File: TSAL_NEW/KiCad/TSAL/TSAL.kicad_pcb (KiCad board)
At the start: 2 copper layers, 74.8 x 40.6 mm, 34 parts, among them J1 HV INPUT, J2 HV GND, J3 Pin Storage, J4 Green_LED_Jp, J5 Conn_02x02_Counter_Clockwise, Q1 BSS84, Q2 BSS84, U1 LTV-817S, U2 LR8K4-G, U4 LM555

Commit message: TSAL Review complete
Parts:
- removed J5: Conn_02x02_Counter_Clockwise, Connector_TE-Connectivity:TE_MATE-N-LOK_1-770874-x_2x02_P4.14mm_Vertical
- added F2: Fuse, TSAL:PCC-1_2-R, F.Cu at (134.9, 90.7)
- added REF**: JUMPER_BLUE, TSAL:JUMPER_BLUE, F.Cu at (153.4, 105.2)
- added Ref**: Val**, TSAL:blinky, B.Cu at (166.9, 109.0)
- added Ref**: Val**, TSAL:zap, B.Cu at (125.5, 91.9)
- added Ref**: Val**, TSAL:zap, F.Cu at (128.0, 98.6)
- J1, J2: footprint Connector_TE-Connectivity:TE_MATE-N-LOK_1-770866-x_1x02_P4.14mm_Vertical -> TSAL:TE_MATE-N-LOK_1-770866-x_1x02_P4.14mm_Vertical
- J3: value Pin Storage -> Conn_01x03; footprint Connector_PinHeader_2.54mm:PinHeader_1x02_P2.54mm_Vertical -> Connector_PinHeader_2.54mm:PinHeader_1x03_P2.54mm_Vertical
- J4: value Green_LED_Jp -> Conn_01x04; footprint Connector_PinHeader_2.54mm:PinHeader_1x02_P2.54mm_Vertical -> TSAL:JST_XH_B4B-XH-AM_1x04_P2.50mm_Vertical
- moved J4 15.1 mm to (162.6, 91.4), turned to 180 degrees
- moved J3 11.6 mm to (153.4, 105.2), turned to 90 degrees
- moved C6 7.18 mm to (155.0, 117.9), turned to 180 degrees
- moved R11 4.61 mm to (163.1, 110.5)
- moved C1 3.78 mm to (125.2, 110.2), turned to 180 degrees
- moved U2 3.05 mm to (135.1, 99.1)
- moved R1 1.71 mm to (129.3, 115.0)
- moved R8 1.69 mm to (150.6, 113.5)
- moved R4 1.14 mm to (131.1, 104.1)
- moved H2 0.76 mm to (113.8, 105.9)
- moved R2 0.32 mm to (144.0, 122.7), turned to 90 degrees
- moved C4 0.25 mm to (163.3, 122.9)
- moved C5 0.25 mm to (165.3, 122.9)
- moved H1 0.10 mm to (144.5, 105.9)
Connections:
- net Net-(D1-Pad2) renamed /FUSE+
- net Net-(D3-Pad1) renamed /LGR_D
- net Net-(Q1-Pad1) renamed /LGR_G+
- net Net-(R1-Pad2) renamed /OPT+
- net Net-(R3-Pad2) renamed /ADJ
- J3 pad 1: Net-(J3-Pad1) -> /LED_GREEN+
- J3 pad 2: Net-(J3-Pad2) -> /LED_GREEN_OUT
- J4 pad 1: /LED_GREEN_OUT -> /GLV+
- J4 pad 2: /LED_GREEN+ -> /LED_RED+
- U2 pad 1: /HV+ -> /HV+F
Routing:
- net GND: track 0.00 -> 53.0 mm, vias 9 -> 14
- net GNDA: track 47.4 -> 39.9 mm
- net /HV+F: track 0.00 -> 7.42 mm
- net /LED_GREEN+: track 8.44 -> 15.4 mm
- net /GLV+: track 11.8 -> 6.73 mm
- net /ADJ: track 10.8 -> 7.58 mm
- net /LGR_D: track 8.53 -> 10.8 mm
- net /OPT+: track 4.01 -> 5.95 mm
- net /LGR_G+: track 4.93 -> 3.91 mm
- net /12V_CAP: track 32.0 -> 32.9 mm
- net /FUSE+: track 6.34 -> 7.26 mm
- net /HV_PRES: track 12.3 -> 11.7 mm
- net +12V: track 76.3 -> 76.8 mm
- net /LED_GREEN_OUT: track 9.04 -> 8.52 mm
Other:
- board size 74.8 x 40.6 mm -> 74.9 x 40.6 mm
- net class HIGH_CUR added: clearance 0.2, trace_width 0.5, via_dia 0.8, via_drill 0.4
- board text added: "GND GRN+ RED+ GLV+"
- board text added: "Green Control"
- board text added: "OFF"
- board text added: "ON"
- board text added: "min. clearance"

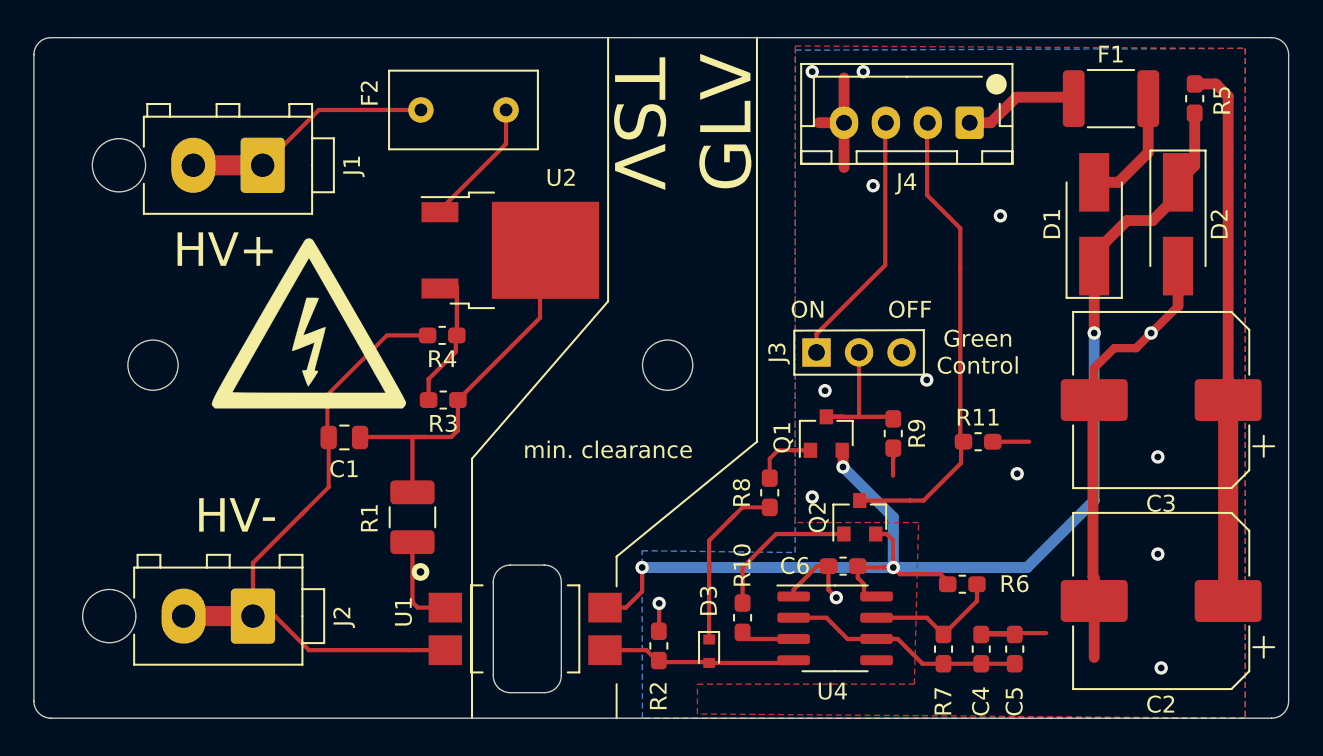
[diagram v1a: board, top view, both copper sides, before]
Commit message: other edits (fix tracks that ran into pads at angles)
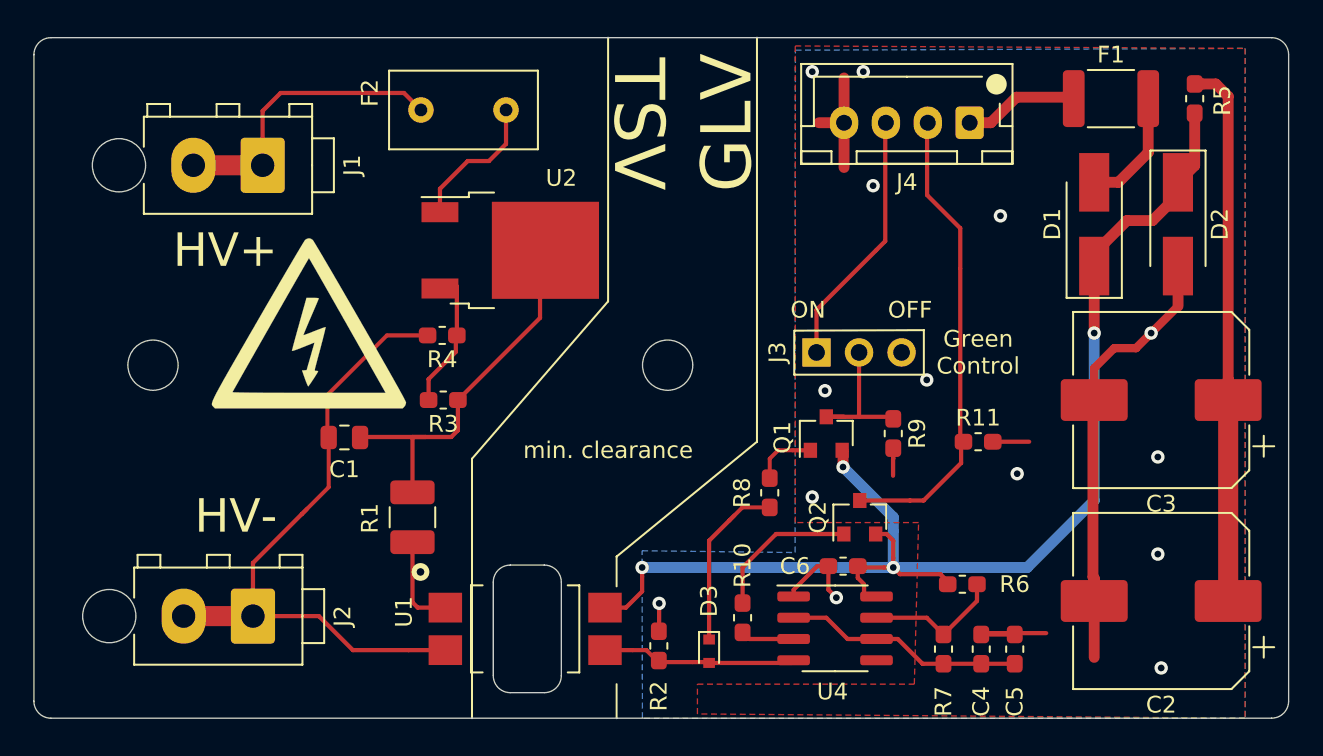
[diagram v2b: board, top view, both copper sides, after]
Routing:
- net /HV+: track 14.9 -> 17.7 mm
- net GNDA: track 39.9 -> 41.2 mm
- net /HV+F: track 7.42 -> 8.48 mm
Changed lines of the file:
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@@
     (thickness 1.6)
     (drawings 46)
-    (tracks 183)
+    (tracks 190)
     (zones 0)
     (modules 38)
@@
   (page A4)
   (layers
-    (0 F.Cu signal hide)
-    (31 B.Cu signal hide)
+    (0 F.Cu signal)
+    (31 B.Cu signal)
     (32 B.Adhes user hide)
     (33 F.Adhes user hide)
@@
   )
   (setup
-    (last_trace_width 0.25)
+    (last_trace_width 0.254)
     (user_trace_width 0.24)
     (user_trace_width 0.254)
@@
       (usegerberextensions true)
       (usegerberattributes true)
-      (usegerberadvancedattributes false)
+      (usegerberadvancedattributes true)
       (creategerberjobfile true)
       (excludeedgelayer true)
@@
   (segment (start 158.27 122.27) (end 159.75 123.75) (width 0.254) (layer F.Cu) (net 2))
   (segment (start 116.2 93.98) (end 120.34 93.98) (width 1.2) (layer F.Cu) (net 3))
-  (segment (start 129.794 90.678) (end 123.698 90.678) (width 0.254) (layer F.Cu) (net 3))
-  (segment (start 123.698 90.678) (end 120.396 93.98) (width 0.254) (layer F.Cu) (net 3))
+  (segment (start 120.34 93.98) (end 120.34 90.734) (width 0.254) (layer F.Cu) (net 3))
+  (segment (start 120.34 90.734) (end 121.412 89.662) (width 0.254) (layer F.Cu) (net 3))
+  (segment (start 121.412 89.662) (end 128.778 89.662) (width 0.254) (layer F.Cu) (net 3))
+  (segment (start 128.778 89.662) (end 129.794 90.678) (width 0.254) (layer F.Cu) (net 3))
   (segment (start 115.621 120.904) (end 119.761 120.904) (width 1.2) (layer F.Cu) (net 4))
-  (segment (start 123.113 122.936) (end 129.052 122.936) (width 0.254) (layer F.Cu) (net 4))
-  (segment (start 121.081 120.904) (end 123.113 122.936) (width 0.254) (layer F.Cu) (net 4))
-  (segment (start 129.052 122.936) (end 131.252 122.936) (width 0.254) (layer F.Cu) (net 4))
   (segment (start 121.081 120.904) (end 119.761 120.904) (width 0.254) (layer F.Cu) (net 4))
   (segment (start 119.971 120.904) (end 119.761 120.904) (width 0.254) (layer F.Cu) (net 4))
@@
   (segment (start 130.189 104.14) (end 127.762 104.14) (width 0.254) (layer F.Cu) (net 4))
   (segment (start 127.762 104.14) (end 124.206 107.696) (width 0.24) (layer F.Cu) (net 4))
-  (segment (start 157.521201 99.946799) (end 157.521201 91.481201) (width 0.254) (layer F.Cu) (net 5))
-  (segment (start 153.416 105.156) (end 153.416 104.052) (width 0.254) (layer F.Cu) (net 5))
-  (segment (start 153.416 104.052) (end 157.521201 99.946799) (width 0.254) (layer F.Cu) (net 5))
+  (segment (start 129.052 122.936) (end 131.252 122.936) (width 0.254) (layer F.Cu) (net 4))
+  (segment (start 125.73 122.936) (end 129.052 122.936) (width 0.254) (layer F.Cu) (net 4))
+  (segment (start 119.761 120.904) (end 123.698 120.904) (width 0.254) (layer F.Cu) (net 4))
+  (segment (start 123.698 120.904) (end 125.73 122.936) (width 0.254) (layer F.Cu) (net 4))
   (segment (start 157.521201 91.481201) (end 157.48 91.44) (width 0.254) (layer F.Cu) (net 5))
+  (segment (start 156.972 99.06) (end 157.521201 98.510799) (width 0.254) (layer F.Cu) (net 5))
+  (segment (start 153.416 102.616) (end 156.972 99.06) (width 0.254) (layer F.Cu) (net 5))
+  (segment (start 153.416 105.156) (end 153.416 102.616) (width 0.254) (layer F.Cu) (net 5))
+  (segment (start 157.521201 98.510799) (end 157.521201 91.481201) (width 0.254) (layer F.Cu) (net 5))
   (segment (start 156 114) (end 159 114) (width 0.254) (layer F.Cu) (net 6))
   (segment (start 159 114) (end 159.812 114) (width 0.254) (layer F.Cu) (net 6))
@@
   (segment (start 131.875 105.125) (end 131.875 104.189) (width 0.254) (layer F.Cu) (net 22))
   (segment (start 134.874 90.678) (end 134.874 92.71) (width 0.254) (layer F.Cu) (net 23))
-  (segment (start 134.874 92.71) (end 131.064 96.52) (width 0.254) (layer F.Cu) (net 23))
+  (segment (start 130.928 96.78) (end 130.928 95.386) (width 0.254) (layer F.Cu) (net 23))
+  (segment (start 130.928 95.386) (end 132.588 93.726) (width 0.254) (layer F.Cu) (net 23))
+  (segment (start 133.858 93.726) (end 134.874 92.71) (width 0.254) (layer F.Cu) (net 23))
+  (segment (start 132.588 93.726) (end 133.858 93.726) (width 0.254) (layer F.Cu) (net 23))
   (zone (net 1) (net_name GND) (layer B.Cu) (hatch edge 0.508)
     (connect_pads (clearance 0.508))
